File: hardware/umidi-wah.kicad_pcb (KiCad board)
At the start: 2 copper layers, 129 x 107 mm, 92 parts, among them J1 Power, J10 Midi_thru, J11 Midi_t/o, J12 Midi_out, J2 Pots Main, J3 Pots Front, J4 Switch, J5 Input, J6 Output, J7 Conn_02x05_Odd_Even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

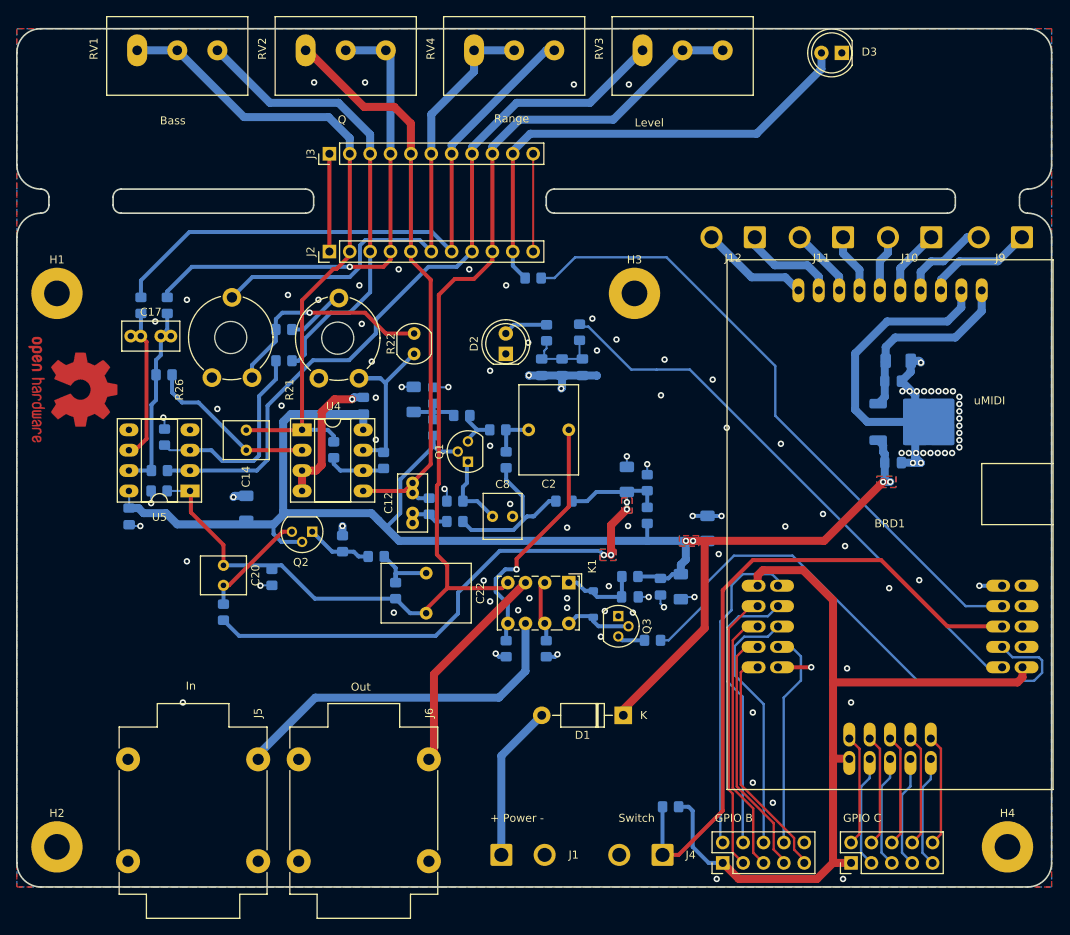
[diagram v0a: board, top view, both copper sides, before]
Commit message: Reduce pcb width to 128mm
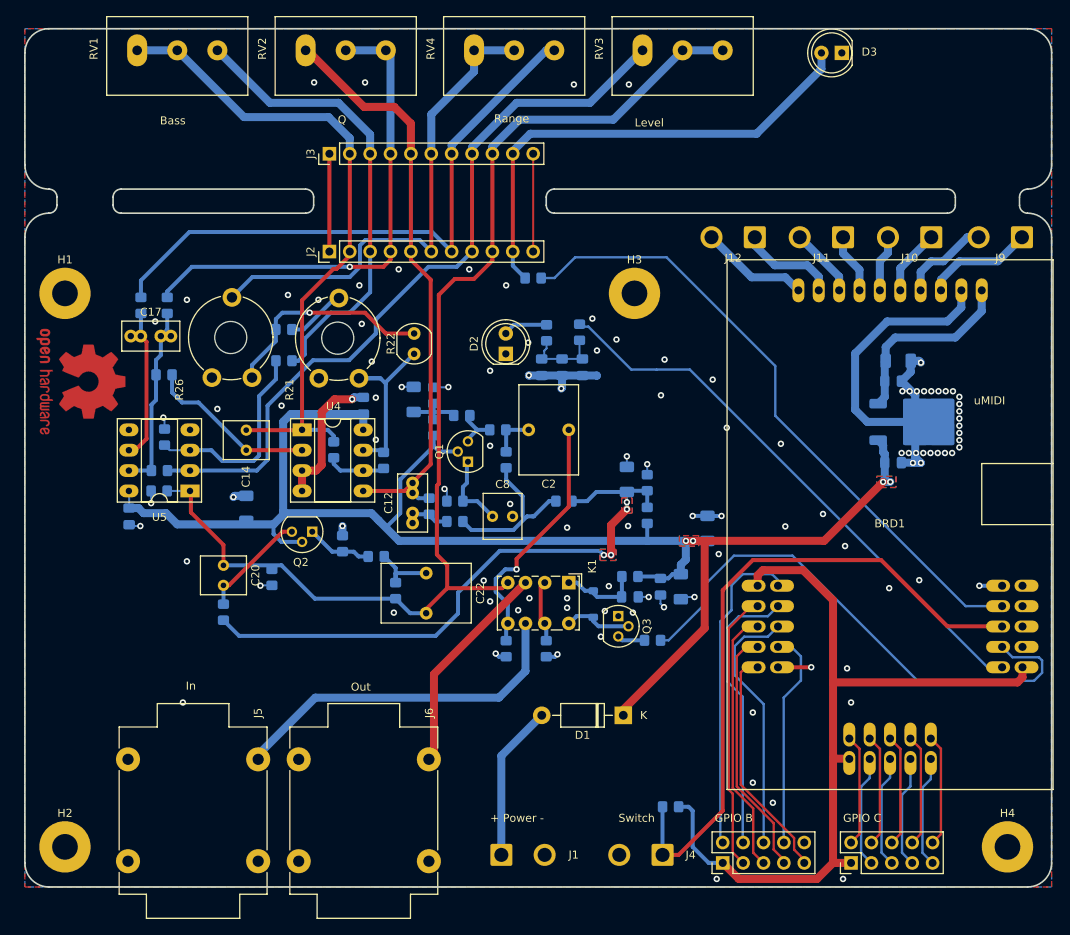
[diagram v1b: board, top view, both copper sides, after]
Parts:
- moved REF** 1.41 mm to (70.0, 74.0)
- moved H1 1.00 mm to (68.0, 63.0)
- moved H2 1.00 mm to (68.0, 132.0)
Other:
- board size 129 x 107 mm -> 128 x 107 mm

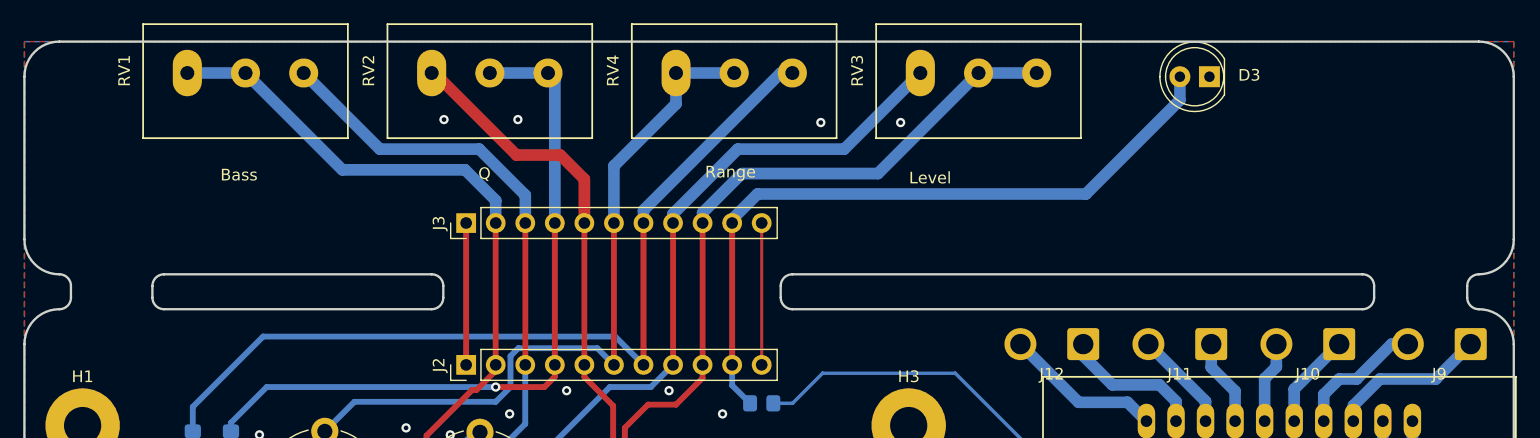
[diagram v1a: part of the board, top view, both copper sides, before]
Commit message: Shrink potentiometer board
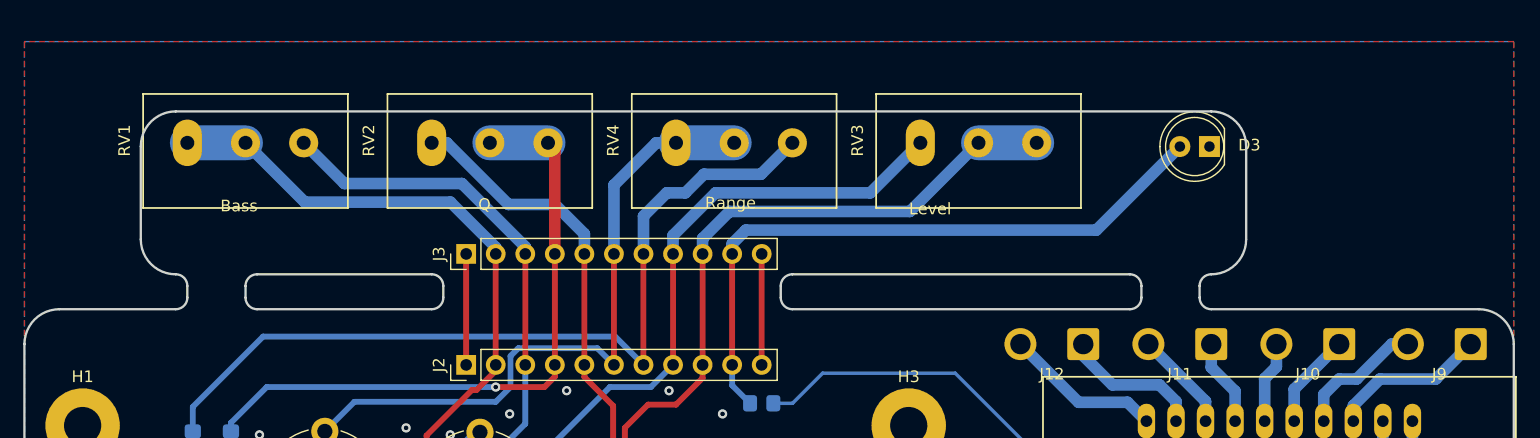
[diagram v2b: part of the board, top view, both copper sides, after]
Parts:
- moved D3 6.00 mm to (164.8, 39.0)
- moved RV1 6.00 mm to (77.0, 38.7)
- moved RV2 6.00 mm to (98.0, 38.7)
- moved RV3 6.00 mm to (140.0, 38.7)
- moved RV4 6.00 mm to (119.0, 38.7)
- moved J3 2.66 mm to (101.0, 48.2)
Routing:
- net GND: track 153.3 -> 148.0 mm, vias 108 -> 104
- net /Filter/rv2_2: track 61.6 -> 56.4 mm
- net /Filter/rv1_2: track 58.1 -> 53.0 mm
- net /Filter/rv2_1: track 74.4 -> 69.4 mm
- net /Filter/rv4_1: track 62.3 -> 57.3 mm
- net /Filter/rv1_1: track 82.5 -> 77.6 mm
- net Net-(D3-A): track 61.2 -> 56.6 mm
- net /wah_out: track 147.2 -> 143.4 mm
- net /Filter/rv3_1: track 96.4 -> 92.9 mm
- net /Filter/rv4_2: track 75.3 -> 72.5 mm
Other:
- board size 128 x 107 mm -> 128 x 101 mm
- board text added: "Status"

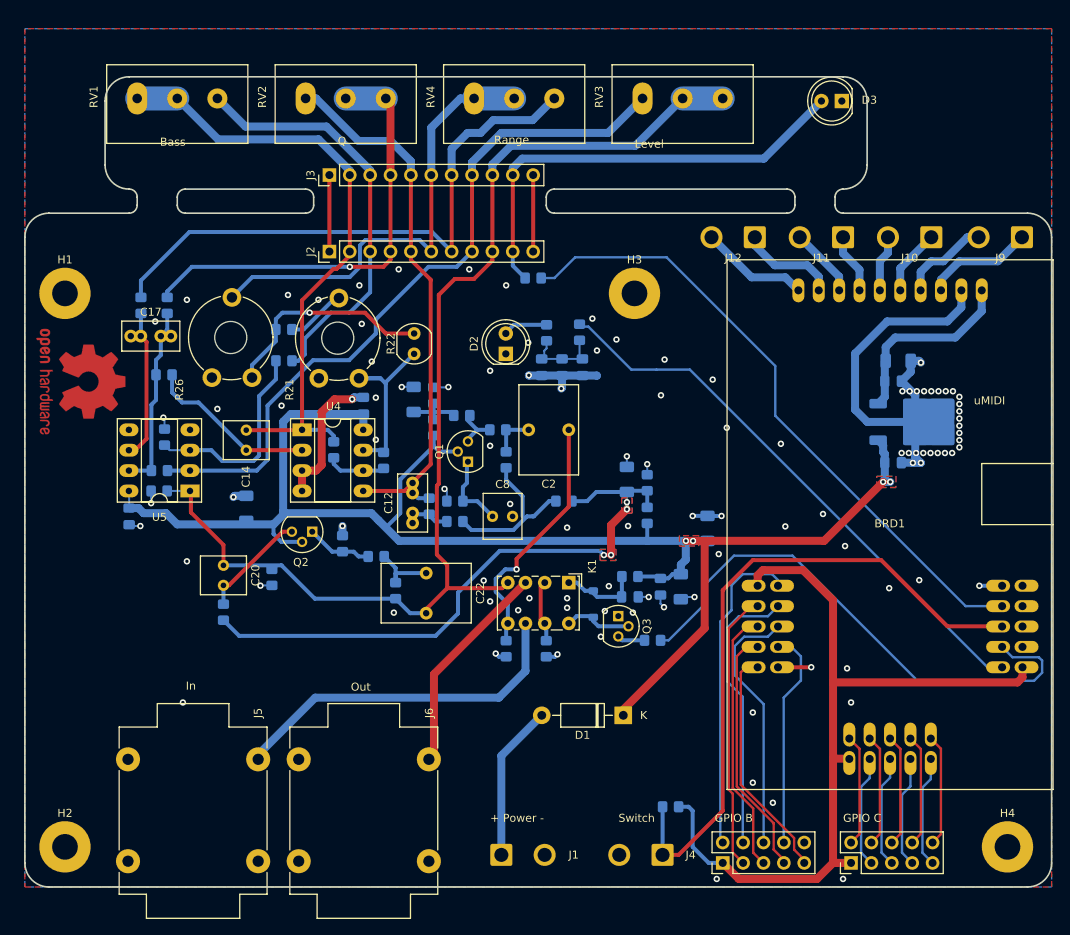
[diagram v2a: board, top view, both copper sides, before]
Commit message: Add mounting holes for umidi module
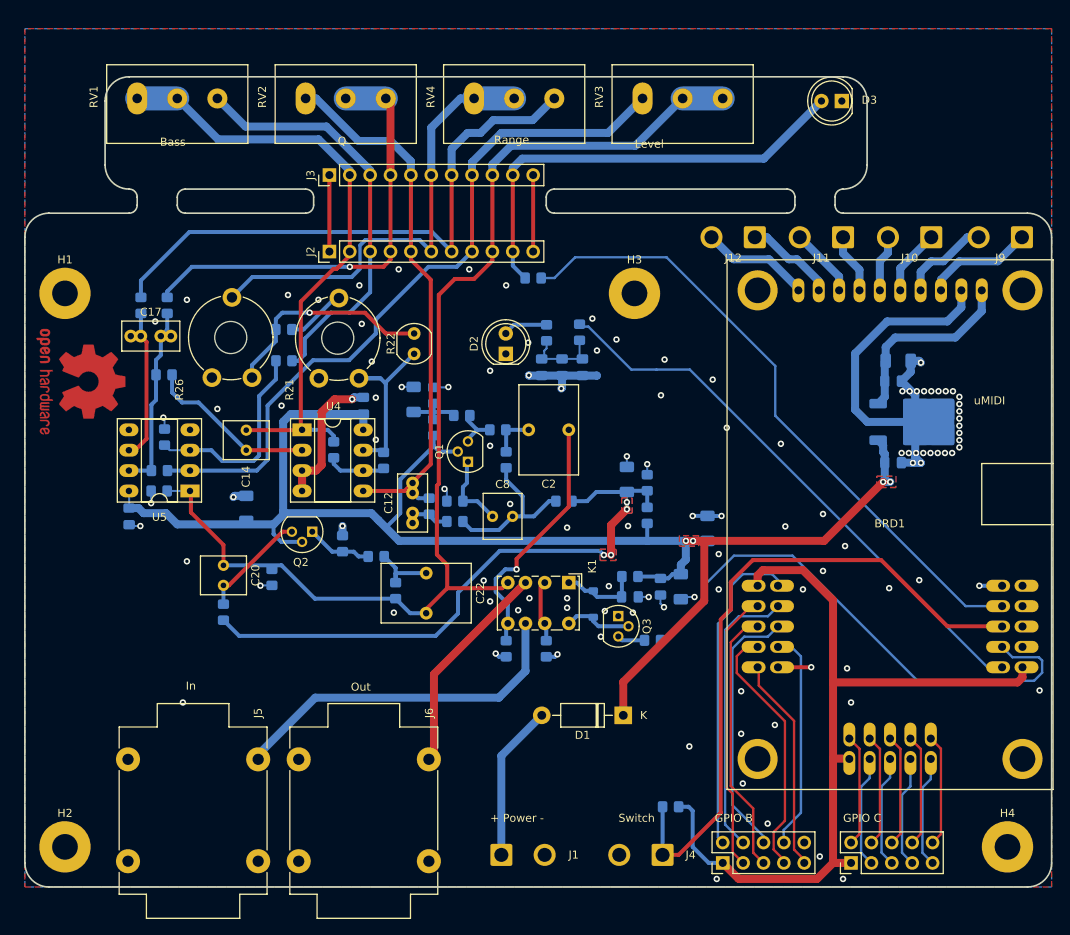
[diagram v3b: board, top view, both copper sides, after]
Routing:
- net Net-(BRD1B-PA7(ADC7)): track 29.4 -> 26.8 mm
- net Net-(BRD1B-PA5(ADC5)): track 31.3 -> 32.4 mm
- net Net-(BRD1A-MIDI_out+): track 12.3 -> 11.4 mm
- net GND: vias 104 -> 112
